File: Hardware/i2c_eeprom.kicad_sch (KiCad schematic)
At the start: 3 parts, among them U11 25LCxxx

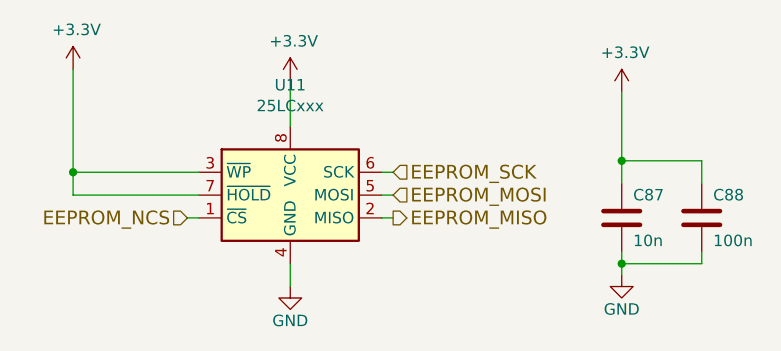
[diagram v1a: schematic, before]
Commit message: feat: updated amplifier IC, finalized design
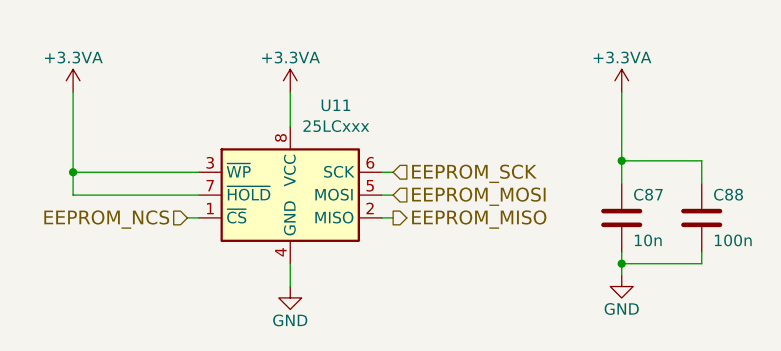
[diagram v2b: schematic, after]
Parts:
- C87, C88: footprint Capacitor_SMD:C_0603_1608Metric_Pad1.08x0.95mm_HandSolder -> Capacitor_SMD:C_0402_1005Metric
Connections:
- net +3V3 renamed +3.3VA
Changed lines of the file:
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@@
     (stroke (width 0) (type default) (color 0 0 0 0))
   )
-  (wire (pts (xy 68.58 50.8) (xy 68.58 45.72))
+  (wire (pts (xy 68.58 50.8) (xy 68.58 46.99))
     (stroke (width 0) (type default) (color 0 0 0 0))
   )
@@
     (stroke (width 0) (type default) (color 0 0 0 0))
   )
-  (wire (pts (xy 44.45 44.45) (xy 44.45 55.88))
+  (wire (pts (xy 44.45 46.99) (xy 44.45 55.88))
     (stroke (width 0) (type default) (color 0 0 0 0))
   )
@@
   (symbol (lib_id "Memory_EEPROM:25LCxxx") (at 68.58 58.42 0) (unit 1)
     (in_bom yes) (on_board yes)
-    (property "Reference" "U11" (id 0) (at 68.58 46.2026 0))
-    (property "Value" "25LCxxx" (id 1) (at 68.58 48.514 0))
+    (property "Reference" "U11" (id 0) (at 73.66 48.4886 0))
+    (property "Value" "25LCxxx" (id 1) (at 73.66 50.8 0))
     (property "Footprint" "Package_SO:SOIC-8_5.275x5.275mm_P1.27mm" (id 2) (at 68.58 58.42 0)
       (effects (font (size 1.27 1.27)) hide)
@@
       (effects (font (size 1.27 1.27)) (justify left))
     )
-    (property "Footprint" "Capacitor_SMD:C_0603_1608Metric_Pad1.08x0.95mm_HandSolder" (id 2) (at 97.79 57.404 90)
+    (property "Footprint" "Capacitor_SMD:C_0402_1005Metric" (id 2) (at 97.79 57.404 90)
       (effects (font (size 1.27 1.27)) hide)
     )
@@
       (effects (font (size 1.27 1.27)) (justify left))
     )
-    (property "Footprint" "Capacitor_SMD:C_0603_1608Metric_Pad1.08x0.95mm_HandSolder" (id 2) (at 106.68 57.404 90)
+    (property "Footprint" "Capacitor_SMD:C_0402_1005Metric" (id 2) (at 106.68 57.404 90)
       (effects (font (size 1.27 1.27)) hide)
     )
@@
     (pin "1")
   )
-  (symbol (lib_id "power:+3.3V") (at 105.41 46.99 0) (unit 1)
-    (in_bom yes) (on_board yes)
-    (property "Reference" "#PWR0109" (id 0) (at 105.41 50.8 0)
-      (effects (font (size 1.27 1.27)) hide)
-    )
-    (property "Value" "+3.3V" (id 1) (at 105.791 42.5958 0))
-    (property "Footprint" "" (id 2) (at 105.41 46.99 0)
-      (effects (font (size 1.27 1.27)) hide)
-    )
-    (property "Datasheet" "" (id 3) (at 105.41 46.99 0)
-      (effects (font (size 1.27 1.27)) hide)
-    )
-    (pin "1")
-  )
-  (symbol (lib_id "power:+3.3V") (at 68.58 45.72 0) (unit 1)
-    (in_bom yes) (on_board yes)
-    (property "Reference" "#PWR0107" (id 0) (at 68.58 49.53 0)
-      (effects (font (size 1.27 1.27)) hide)
-    )
-    (property "Value" "+3.3V" (id 1) (at 68.961 41.3258 0))
-    (property "Footprint" "" (id 2) (at 68.58 45.72 0)
-      (effects (font (size 1.27 1.27)) hide)
-    )
-    (property "Datasheet" "" (id 3) (at 68.58 45.72 0)
-      (effects (font (size 1.27 1.27)) hide)
-    )
-    (pin "1")
-  )
   (symbol (lib_id "power:GND") (at 68.58 68.58 0) (unit 1)
     (in_bom yes) (on_board yes)
@@
     (pin "1")
   )
-  (symbol (lib_id "power:+3.3V") (at 44.45 44.45 0) (unit 1)
+  (symbol (lib_id "power:+3.3VA") (at 44.45 46.99 0) (unit 1)
     (in_bom yes) (on_board yes)
-    (property "Reference" "#PWR0106" (id 0) (at 44.45 48.26 0)
+    (property "Reference" "#PWR0106" (id 0) (at 44.45 50.8 0)
       (effects (font (size 1.27 1.27)) hide)
     )
-    (property "Value" "+3.3V" (id 1) (at 44.831 40.0558 0))
-    (property "Footprint" "" (id 2) (at 44.45 44.45 0)
+    (property "Value" "+3.3VA" (id 1) (at 44.45 43.18 0))
+    (property "Footprint" "" (id 2) (at 44.45 46.99 0)
       (effects (font (size 1.27 1.27)) hide)
     )
-    (property "Datasheet" "" (id 3) (at 44.45 44.45 0)
+    (property "Datasheet" "" (id 3) (at 44.45 46.99 0)
       (effects (font (size 1.27 1.27)) hide)
     )
+    (pin "1")
+  )
+  (symbol (lib_id "power:+3.3VA") (at 68.58 46.99 0) (unit 1)
+    (in_bom yes) (on_board yes)
+    (property "Reference" "#PWR0109" (id 0) (at 68.58 50.8 0)
+      (effects (font (size 1.27 1.27)) hide)
+    )
+    (property "Value" "+3.3VA" (id 1) (at 68.58 43.18 0))
+    (property "Footprint" "" (id 2) (at 68.58 46.99 0)
+      (effects (font (size 1.27 1.27)) hide)
+    )
+    (property "Datasheet" "" (id 3) (at 68.58 46.99 0)
+      (effects (font (size 1.27 1.27)) hide)
+    )
+    (pin "1")
+  )
+  (symbol (lib_id "power:+3.3VA") (at 105.41 46.99 0) (unit 1)
+    (in_bom yes) (on_board yes)
+    (property "Reference" "#PWR0107" (id 0) (at 105.41 50.8 0)
+      (effects (font (size 1.27 1.27)) hide)
+    )
+    (property "Value" "+3.3VA" (id 1) (at 105.41 43.18 0))
+    (property "Footprint" "" (id 2) (at 105.41 46.99 0)
+      (effects (font (size 1.27 1.27)) hide)
+    )
+    (property "Datasheet" "" (id 3) (at 105.41 46.99 0)
+      (effects (font (size 1.27 1.27)) hide)
+    )

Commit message: prod. version blus mini a
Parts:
- C66: renamed from C88; MPN (none) -> C307331; Mfr.Nr. GRM31CR71H475KA12L -> (none)
- C69: renamed from C87; MPN (none) -> C15195; Mfr.Nr. GRM31CR71H475KA12L -> (none)
- renumbered U11 to U9
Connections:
- net +3.3VA renamed +3.3V
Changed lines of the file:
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@@
   (symbol (lib_id "Memory_EEPROM:25LCxxx") (at 68.58 58.42 0) (unit 1)
     (in_bom yes) (on_board yes)
-    (property "Reference" "U11" (id 0) (at 73.66 48.4886 0))
+    (property "Reference" "U9" (id 0) (at 73.66 48.4886 0))
     (property "Value" "25LCxxx" (id 1) (at 73.66 50.8 0))
     (property "Footprint" "Package_SO:SOIC-8_5.275x5.275mm_P1.27mm" (id 2) (at 68.58 58.42 0)
@@
     )
     (property "Datasheet" "http://ww1.microchip.com/downloads/en/DeviceDoc/21832H.pdf" (id 3) (at 68.58 58.42 0)
+      (effects (font (size 1.27 1.27)) hide)
+    )
+    (property "Mfr.Nr." "" (id 4) (at 68.58 58.42 0)
       (effects (font (size 1.27 1.27)) hide)
     )
@@
   (symbol (lib_id "Device:C") (at 105.41 60.96 0) (unit 1)
     (in_bom yes) (on_board yes)
-    (property "Reference" "C87" (id 0) (at 106.68 58.42 0)
+    (property "Reference" "C69" (id 0) (at 106.68 58.42 0)
       (effects (font (size 1.27 1.27)) (justify left))
     )
@@
       (effects (font (size 1.27 1.27)) hide)
     )
-    (property "Mfr.Nr." "GRM31CR71H475KA12L" (id 4) (at 105.41 60.96 0)
+    (property "Mfr.Nr." "" (id 4) (at 105.41 60.96 0)
       (effects (font (size 1.524 1.524)) hide)
+    )
+    (property "MPN" "C15195" (id 5) (at 105.41 60.96 0)
+      (effects (font (size 1.27 1.27)) hide)
     )
     (pin "1")
@@
   (symbol (lib_id "Device:C") (at 114.3 60.96 0) (unit 1)
     (in_bom yes) (on_board yes)
-    (property "Reference" "C88" (id 0) (at 115.57 58.42 0)
+    (property "Reference" "C66" (id 0) (at 115.57 58.42 0)
       (effects (font (size 1.27 1.27)) (justify left))
     )
@@
       (effects (font (size 1.27 1.27)) hide)
     )
-    (property "Mfr.Nr." "GRM31CR71H475KA12L" (id 4) (at 114.3 60.96 0)
+    (property "Mfr.Nr." "" (id 4) (at 114.3 60.96 0)
       (effects (font (size 1.524 1.524)) hide)
+    )
+    (property "MPN" "C307331" (id 5) (at 114.3 60.96 0)
+      (effects (font (size 1.27 1.27)) hide)
     )
     (pin "1")
@@
   (symbol (lib_id "power:GND") (at 105.41 67.31 0) (unit 1)
     (in_bom yes) (on_board yes)
-    (property "Reference" "#PWR0110" (id 0) (at 105.41 73.66 0)
+    (property "Reference" "#PWR0136" (id 0) (at 105.41 73.66 0)
       (effects (font (size 1.27 1.27)) hide)
     )
@@
   (symbol (lib_id "power:GND") (at 68.58 68.58 0) (unit 1)
     (in_bom yes) (on_board yes)
-    (property "Reference" "#PWR0108" (id 0) (at 68.58 74.93 0)
+    (property "Reference" "#PWR0140" (id 0) (at 68.58 74.93 0)
       (effects (font (size 1.27 1.27)) hide)
     )
@@
     (pin "1")
   )
-  (symbol (lib_id "power:+3.3VA") (at 44.45 46.99 0) (unit 1)
+  (symbol (lib_id "power:+3.3V") (at 44.45 46.99 0) (unit 1)
     (in_bom yes) (on_board yes)
-    (property "Reference" "#PWR0106" (id 0) (at 44.45 50.8 0)
+    (property "Reference" "#PWR0142" (id 0) (at 44.45 50.8 0)
       (effects (font (size 1.27 1.27)) hide)
     )
-    (property "Value" "+3.3VA" (id 1) (at 44.45 43.18 0))
+    (property "Value" "+3.3V" (id 1) (at 44.45 43.434 0))
     (property "Footprint" "" (id 2) (at 44.45 46.99 0)
       (effects (font (size 1.27 1.27)) hide)
@@
     (pin "1")
   )
-  (symbol (lib_id "power:+3.3VA") (at 68.58 46.99 0) (unit 1)
+  (symbol (lib_id "power:+3.3V") (at 68.58 46.99 0) (unit 1)
     (in_bom yes) (on_board yes)
-    (property "Reference" "#PWR0109" (id 0) (at 68.58 50.8 0)
+    (property "Reference" "#PWR0145" (id 0) (at 68.58 50.8 0)
       (effects (font (size 1.27 1.27)) hide)
     )
-    (property "Value" "+3.3VA" (id 1) (at 68.58 43.18 0))
+    (property "Value" "+3.3V" (id 1) (at 68.58 43.434 0))
     (property "Footprint" "" (id 2) (at 68.58 46.99 0)
       (effects (font (size 1.27 1.27)) hide)
@@
     (pin "1")
   )
-  (symbol (lib_id "power:+3.3VA") (at 105.41 46.99 0) (unit 1)
+  (symbol (lib_id "power:+3.3V") (at 105.41 46.99 0) (unit 1)
     (in_bom yes) (on_board yes)
-    (property "Reference" "#PWR0107" (id 0) (at 105.41 50.8 0)
+    (property "Reference" "#PWR0144" (id 0) (at 105.41 50.8 0)
       (effects (font (size 1.27 1.27)) hide)
     )
-    (property "Value" "+3.3VA" (id 1) (at 105.41 43.18 0))
+    (property "Value" "+3.3V" (id 1) (at 105.41 43.434 0))
     (property "Footprint" "" (id 2) (at 105.41 46.99 0)
       (effects (font (size 1.27 1.27)) hide)

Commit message: feat!: wip, version b
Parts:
- U9: value 25LCxxx -> 25LC512; Mfr.Nr. (none) -> M
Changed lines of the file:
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@@
     (in_bom yes) (on_board yes)
     (property "Reference" "U9" (id 0) (at 73.66 48.4886 0))
-    (property "Value" "25LCxxx" (id 1) (at 73.66 50.8 0))
+    (property "Value" "25LC512" (id 1) (at 73.66 50.8 0))
     (property "Footprint" "Package_SO:SOIC-8_5.275x5.275mm_P1.27mm" (id 2) (at 68.58 58.42 0)
       (effects (font (size 1.27 1.27)) hide)
@@
       (effects (font (size 1.27 1.27)) hide)
     )
-    (property "Mfr.Nr." "" (id 4) (at 68.58 58.42 0)
+    (property "Mfr.Nr." "M" (id 4) (at 68.58 58.42 0)
       (effects (font (size 1.27 1.27)) hide)
     )
